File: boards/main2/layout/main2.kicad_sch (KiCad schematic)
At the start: 25 parts, among them IC1 STM32H725RGV6

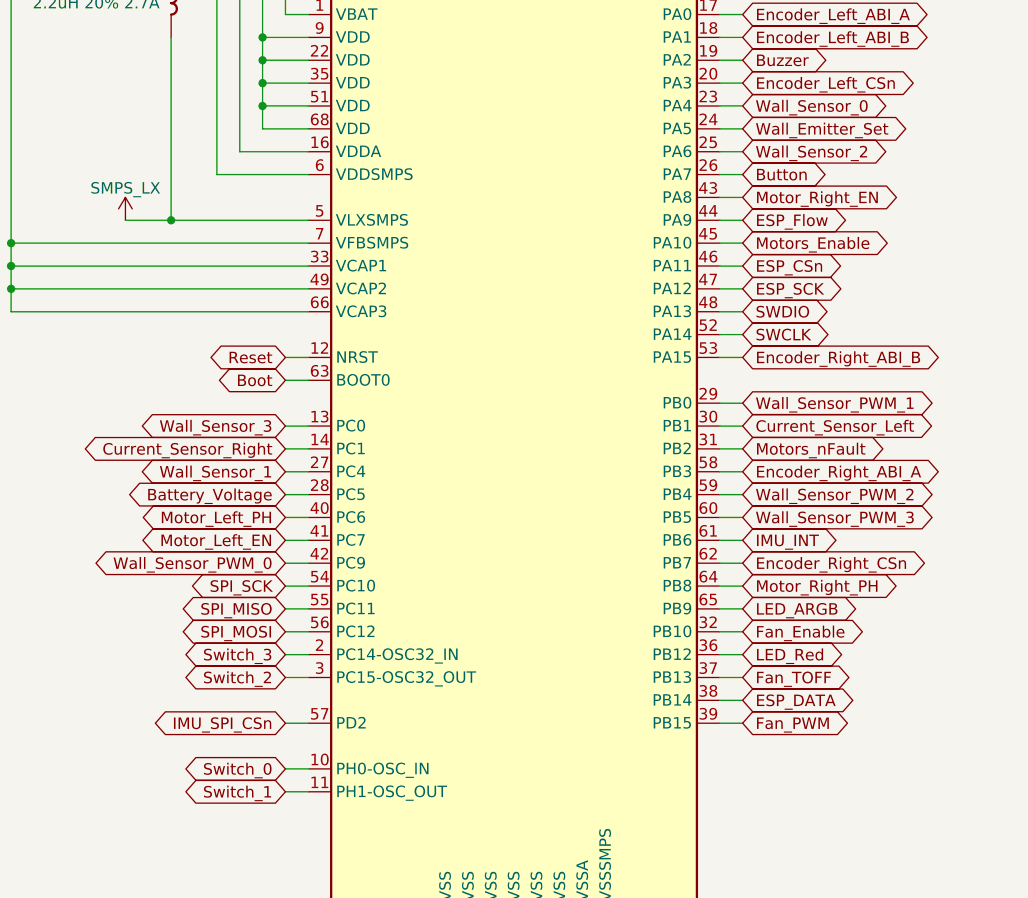
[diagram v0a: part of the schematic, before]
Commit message: 🚧 Move main2's C5 link to SPI3 on the STM32's rear-right face
SPI2's clock exists only on the STM32's left-side pins, so the link had to
cross every line leaving the rear-right face to reach the C5.

- The link moves to SPI3, a 3-wire master on MOSI with no IOSWP: SCK on
  PC10, DATA on PC12, CSn on PC11. The UART4 fallback stays on
  PC10/PC11 (AF8).
- The sensor bus moves to SPI2 on PB13/PB14/PB15.
- Fan_PWM moves to TIM14_CH1 on PA7, with the same 275 MHz clock and
  ARR. Button moves to PA11 and Fan_TOFF to PA12.
- CubeMX 6.18.1 accepts both the SPI and the UART4 configurations.
- Routed: all four link joins and the SPI_SCK join to EC2. DRC shows 0
  errors and 13 unconnected. Button, Fan_TOFF, Encoder_Right_ABI_B and
  Wall_Sensor_PWM_2 are open in the pocket behind the STM32's rear tip.
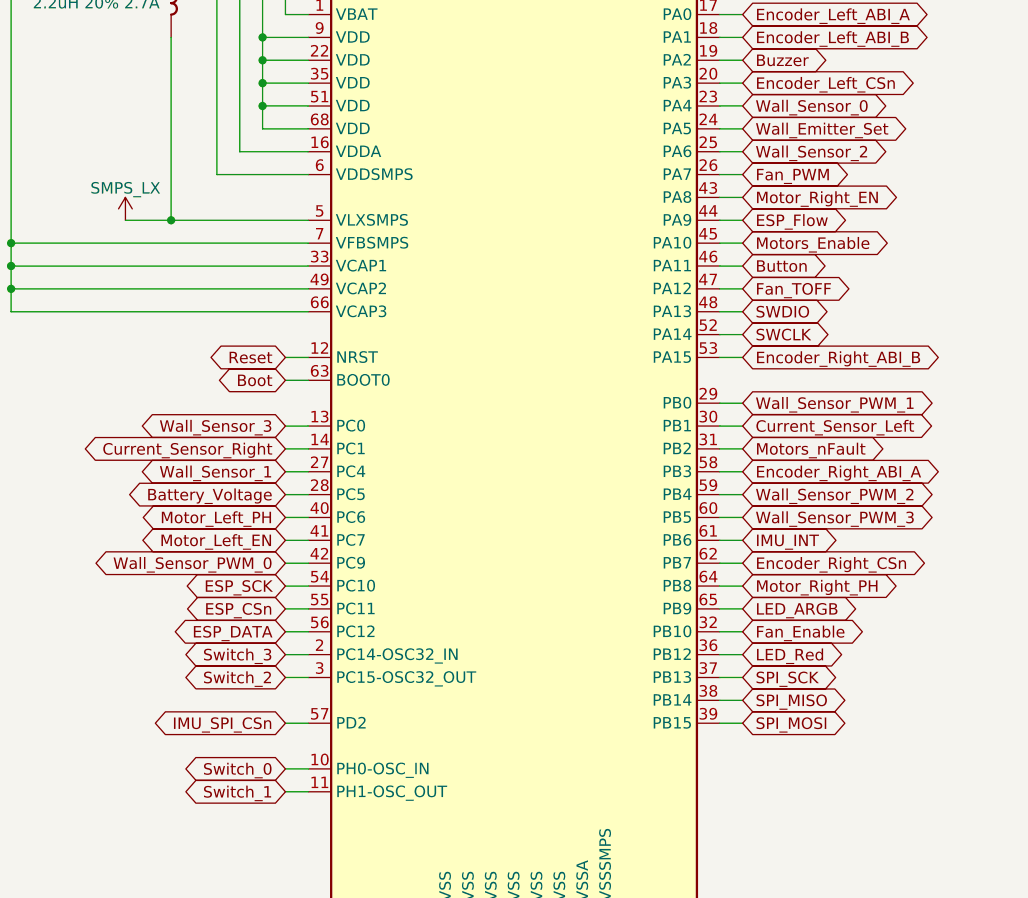
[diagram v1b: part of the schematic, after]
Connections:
- net Button: now also IC1.46 (PA11); no longer IC1.26 (PA7)
- net ESP_CSn: now also IC1.55 (PC11); no longer IC1.46 (PA11)
- net ESP_DATA: now also IC1.56 (PC12); no longer IC1.38 (PB14)
- net ESP_SCK: now also IC1.54 (PC10); no longer IC1.47 (PA12)
- net Fan_PWM: now also IC1.26 (PA7); no longer IC1.39 (PB15)
- net Fan_TOFF: now also IC1.47 (PA12); no longer IC1.37 (PB13)
- net SPI_MISO: now also IC1.38 (PB14); no longer IC1.55 (PC11)
- net SPI_MOSI: now also IC1.39 (PB15); no longer IC1.56 (PC12)
- net SPI_SCK: now also IC1.37 (PB13); no longer IC1.54 (PC10)
